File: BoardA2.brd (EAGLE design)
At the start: 44 x 93 mm, 18 parts, among them J1 FEMALE 2x3, T1 2N2222

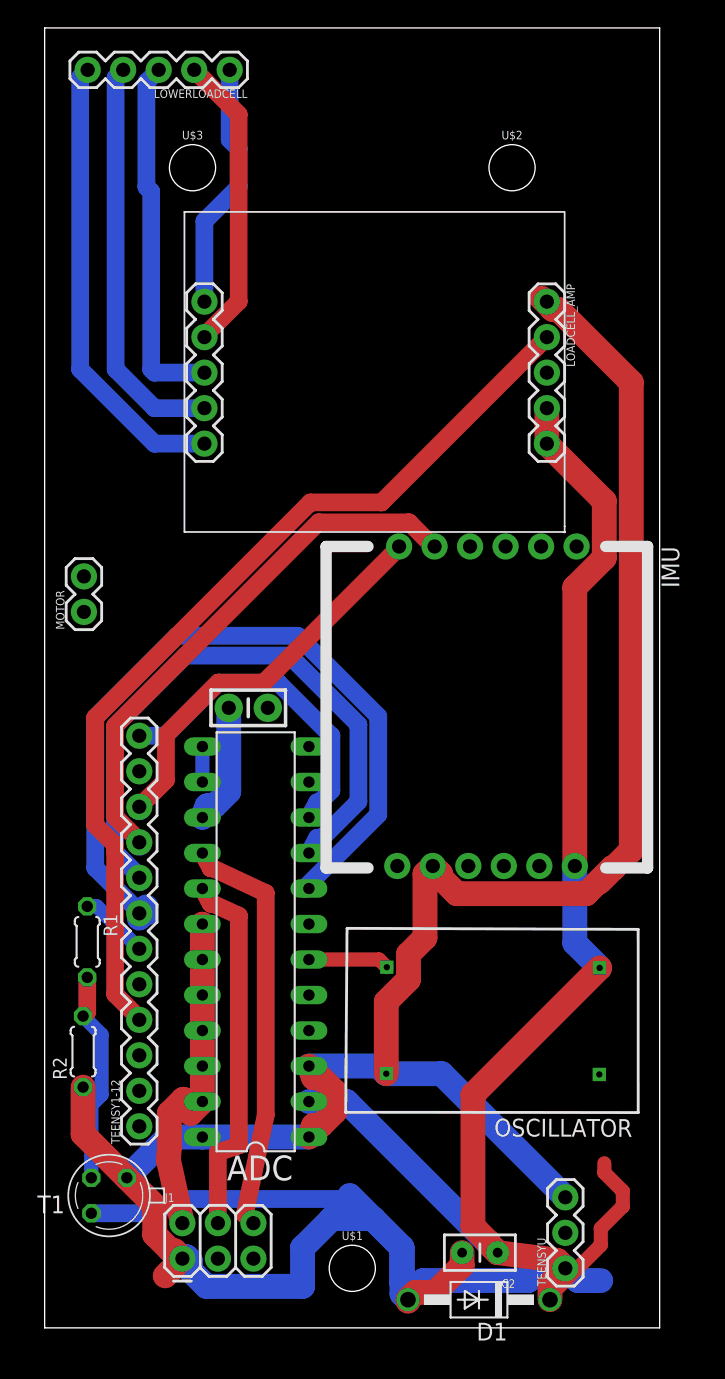
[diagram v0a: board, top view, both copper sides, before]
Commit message: moved connector board 1
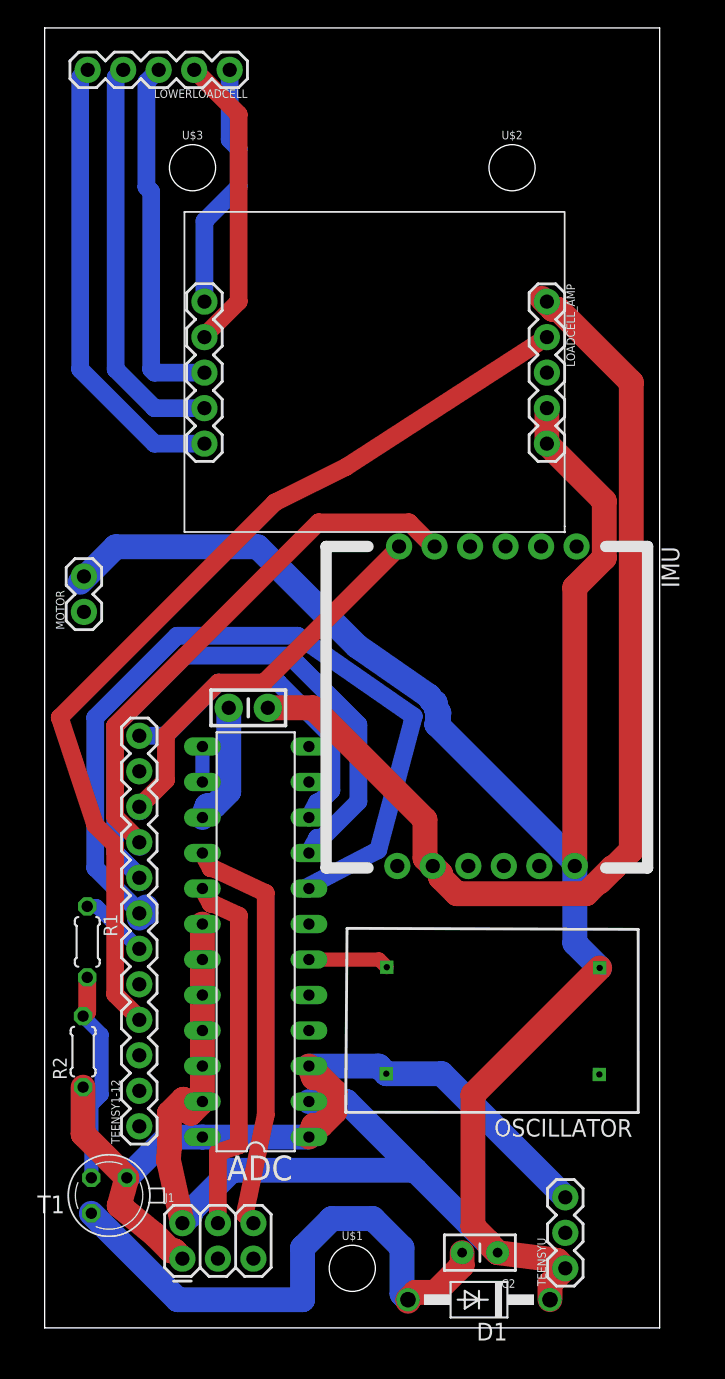
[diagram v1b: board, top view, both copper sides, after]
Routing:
- net 5V: track 158.2 -> 183.4 mm
- net N$6: track 46.0 -> 40.0 mm
- net ADC-TFS: track 56.7 -> 60.0 mm
- net AMP-CLK: track 66.5 -> 67.9 mm
- net GND: track 137.2 -> 137.8 mm

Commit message: Update 2
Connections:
- new net DC-CTRL: J1.2
- net 5V: now also J1.6; no longer J1.2
- net ADC-CH1: now also J1.5; no longer J1.6
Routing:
- net 5V: track 183.4 -> 173.6 mm
- net ADC-CH1: track 29.6 -> 28.7 mm
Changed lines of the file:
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@@
 <dimension x1="0" y1="0" x2="0" y2="93" x3="-13.335" y3="46.5" textsize="1.778" layer="1"/>
 <wire x1="0" y1="93" x2="0" y2="0" width="0" layer="20"/>
-<wire x1="1.5" y1="3.5" x2="42" y2="0.96" width="0.1524" layer="231"/>
+<wire x1="1.5" y1="0.96" x2="42" y2="0.96" width="0.1524" layer="231"/>
 <wire x1="42" y1="0.96" x2="42" y2="91.5" width="0.1524" layer="231"/>
 <wire x1="42" y1="91.5" x2="1.5" y2="91.5" width="0.1524" layer="231"/>
-<wire x1="1.5" y1="91.5" x2="1.5" y2="3.5" width="0.1524" layer="231"/>
+<wire x1="1.5" y1="91.5" x2="1.5" y2="0.96" width="0.1524" layer="231"/>
 </plain>
 <attributes>
@@
 <wire x1="11.287" y1="18.732" x2="11.287" y2="21.272" width="1.778" layer="1"/>
 <wire x1="35.932" y1="63.26" x2="35.932" y2="65.8" width="1.778" layer="1"/>
-<contactref element="J1" pad="2"/>
 <wire x1="11.287" y1="18.732" x2="11.287" y2="16.192" width="1.778" layer="1"/>
 <wire x1="37.93" y1="33.044" x2="37.93" y2="52.97515625" width="1.778" layer="1"/>
@@
 <wire x1="10.4488" y1="15.3538" x2="9.9216875" y2="16.3538" width="1.778" layer="1"/>
 <wire x1="8.9248" y1="12.9470875" x2="8.8552" y2="12.0166875" width="1.778" layer="1"/>
-<wire x1="8.8552" y1="12.0166875" x2="9.8552" y2="7.493" width="1.778" layer="1"/>
 <contactref element="MOTOR" pad="2"/>
-<wire x1="10.414" y1="8.31364375" x2="10.414" y2="8.0518" width="1.778" layer="16"/>
-<wire x1="10.414" y1="8.0518" x2="9.8552" y2="7.493" width="1.778" layer="16"/>
-<wire x1="26.515" y1="11.275" x2="13.37535625" y2="11.275" width="1.778" layer="16"/>
-<wire x1="13.37535625" y1="11.275" x2="10.414" y2="8.31364375" width="1.778" layer="16"/>
 <wire x1="28.1810875" y1="43.3644125" x2="28.12404375" y2="43.6804625" width="1.778" layer="16"/>
 <wire x1="28.12404375" y1="43.6804625" x2="28.20646875" y2="43.990853125" width="1.778" layer="16"/>
@@
 <wire x1="15.24" y1="55.88" x2="5.08" y2="55.88" width="1.778" layer="16"/>
 <wire x1="5.08" y1="55.88" x2="2.54" y2="53.34" width="1.778" layer="16"/>
+<contactref element="J1" pad="6"/>
+<wire x1="26.515" y1="11.275" x2="18.7172" y2="11.275" width="1.524" layer="16"/>
+<wire x1="18.7172" y1="11.275" x2="14.9352" y2="7.493" width="1.524" layer="16"/>
 <wire x1="22.337965625" y1="48.782034375" x2="18.907" y2="41.592" width="0" layer="19" extent="16-16"/>
 <wire x1="2.811" y1="53.763" x2="2.54" y2="53.34" width="0" layer="19" extent="16-16"/>
+<wire x1="8.8552" y1="12.0166875" x2="14.9352" y2="7.493" width="0" layer="19" extent="1-1"/>
 </signal>
 <signal name="N$1">
@@
 <signal name="ADC-CH1">
 <contactref element="ADC" pad="16"/>
-<contactref element="J1" pad="6"/>
 <wire x1="11.287" y1="33.972" x2="11.8792" y2="32.8798" width="1.27" layer="1"/>
 <wire x1="11.8792" y1="32.8798" x2="12.0471" y2="32.8798" width="1.27" layer="1"/>
-<wire x1="14.3176" y1="8.1106" x2="14.9352" y2="7.493" width="1.27" layer="1"/>
 <wire x1="12.0471" y1="32.8798" x2="15.8176" y2="31.1093" width="1.27" layer="1"/>
 <wire x1="15.8176" y1="31.1093" x2="15.8176" y2="15.24" width="1.27" layer="1"/>
 <wire x1="15.8176" y1="15.24" x2="14.3176" y2="8.1106" width="1.27" layer="1"/>
+<contactref element="J1" pad="5"/>
+<wire x1="14.9352" y1="4.953" x2="14.3176" y2="8.1106" width="0" layer="19" extent="1-1"/>
 </signal>
 <signal name="ADC-CH2">
@@
 <wire x1="13.239" y1="85.0107375" x2="13.239" y2="90.002" width="1.27" layer="16"/>
 </signal>
+<signal name="DC-CTRL">
+<contactref element="J1" pad="2"/>
+</signal>
 </signals>

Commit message: Mid board Rerouting 1
Work in progress. Please do not commit any changes to Board2
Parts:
- moved C2 84.2 mm to (40.0, 89.2)
- moved T1 82.7 mm to (30.0, 88.2)
- moved D1 81.4 mm to (36.2, 83.3)
- moved R2 69.9 mm to (25.6, 85.8)
- moved R1 61.1 mm to (20.8, 86.0)
- moved OSCILLATOR 58.8 mm to (23.0, 80.1), turned to 269.8 degrees
- moved MOTOR 43.5 mm to (22.2, 90.2), turned to 0 degrees
- moved LOADCELL_AMP 13.5 mm to (11.7, 64.0), turned to 90 degrees
- moved IMU 12.1 mm to (43.6, 43.8)
- moved TEENSYU 4.21 mm to (33.1, 3.88)
- moved TEENSY1-12 3.84 mm to (3.05, 13.5)
- moved C1 3.23 mm to (14.6, 47.6), turned to 90 degrees
- moved J1 2.54 mm to (7.82, 3.43)
- moved ADC 2.07 mm to (13.6, 29.0), turned to 270 degrees
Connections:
- removed net ADC-SLK: TEENSY1-12.5
- removed net N$11: ADC.4
- removed net TEENSY1: TEENSY1-12.1
- net ADC-SCLK: now also TEENSY1-12.5
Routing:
- net 5V: track 173.6 -> 0.00 mm
- net GND: track 137.8 -> 0.00 mm
- net AMP-CLK: track 67.9 -> 0.00 mm
- net ADC-TFS: track 60.0 -> 0.00 mm
- net ADC-RFS: track 44.0 -> 0.00 mm
- net N$6: track 40.0 -> 0.00 mm
- net IMU-TX: track 38.8 -> 0.00 mm
- net E+: track 32.7 -> 0.00 mm
- net N$5: track 29.1 -> 0.00 mm
- net ADC-CH1: track 28.7 -> 0.00 mm
- net IMU-RX: track 28.4 -> 0.00 mm
- net ADC-CH2: track 26.5 -> 0.00 mm
- net N$7: track 25.8 -> 0.00 mm
- net ADC-DOUT: track 23.4 -> 0.00 mm
- net N$9: track 21.5 -> 0.00 mm
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
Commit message: rerouting 2
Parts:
- moved OSCILLATOR 62.1 mm to (32.1, 18.6), turned to 179.8 degrees
- moved C1 37.4 mm to (19.6, 10.5)
- moved IMU 27.6 mm to (21.3, 27.6), turned to 90 degrees
- moved D1 8.27 mm to (34.6, 75.2)
- moved TEENSYU 4.21 mm to (37.2, 4.26)
- moved R2 4.10 mm to (23.6, 82.2)
- moved TEENSY1-12 3.84 mm to (6.77, 14.4)
- moved R1 3.21 mm to (19.8, 83.0)
- moved MOTOR 2.54 mm to (19.7, 90.2)
- moved ADC 1.83 mm to (15.1, 30.0)
- moved T1 1.14 mm to (29.0, 87.7)
- moved LOADCELL_AMP 1.02 mm to (12.7, 64.0)
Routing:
- net GND: track 0.00 -> 176.6 mm
- net 5V: track 0.00 -> 168.3 mm
- net MOTOR: track 0.00 -> 73.3 mm, vias 0 -> 2
- net IMU-RX: track 0.00 -> 59.1 mm
- net AMP-DAT: track 0.00 -> 50.7 mm, vias 0 -> 1
- net IMU-TX: track 0.00 -> 48.7 mm, vias 0 -> 1
- net ADC-DIN: track 0.00 -> 44.6 mm, vias 0 -> 1
- net AMP-CLK: track 0.00 -> 41.5 mm
- net N$4: track 0.00 -> 37.6 mm, vias 0 -> 1
- net ADC-RFS: track 0.00 -> 36.7 mm
- net N$6: track 0.00 -> 32.6 mm
- net ADC-CH1: track 0.00 -> 24.8 mm
- net N$3: track 0.00 -> 23.7 mm, vias 0 -> 1
- net ADC-CH2: track 0.00 -> 22.9 mm
- net N$7: track 0.00 -> 16.9 mm
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
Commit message: update 2
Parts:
- moved C1 2.74 mm to (17.1, 9.49), turned to 180 degrees
- moved J1 0.77 mm to (7.35, 2.83)
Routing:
- net 5V: track 168.3 -> 214.4 mm
- net ADC-DOUT: track 0.16 -> 32.3 mm, vias 0 -> 1
- net N$3: track 23.7 -> 14.9 mm, vias 1 -> 0
- net ADC-CH1: track 24.8 -> 31.2 mm
- net GND: track 176.6 -> 180.3 mm
- net N$4: track 37.6 -> 34.6 mm
- net AMP-DAT: track 50.7 -> 52.3 mm
- net ADC-CH2: track 22.9 -> 23.5 mm

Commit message: update3
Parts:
- moved MOTOR 2.25 mm to (20.2, 88.0)
- moved LOWERLOADCELL 2.00 mm to (13.2, 88.0)
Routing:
- net N$7: track 16.9 -> 14.1 mm
- net N$5: track 14.8 -> 12.8 mm
- net E+: track 14.8 -> 12.8 mm
- net N$9: track 14.8 -> 13.0 mm
- net N$10: track 14.8 -> 13.6 mm
- net N$6: track 32.6 -> 31.9 mm
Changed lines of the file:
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@@
 <element name="D1" library="diode" library_urn="urn:adsk.eagle:library:210" package="DO41-10" value="1N4004" x="34.63" y="75.168" rot="R180"/>
 <element name="C2" library="SparkFun-Passives" package="CAP-PTH-SMALL2" value="0.1uf" x="40.028" y="89.202" rot="R180"/>
-<element name="MOTOR" library="SparkFun-Connectors" package="1X02" value="" x="19.683" y="90.189"/>
-<element name="LOWERLOADCELL" library="SparkFun-Connectors" package="1X05" value="" x="13.239" y="90.002" rot="R180"/>
+<element name="MOTOR" library="SparkFun-Connectors" package="1X02" value="" x="20.191" y="88"/>
+<element name="LOWERLOADCELL" library="SparkFun-Connectors" package="1X05" value="" x="13.239" y="88" rot="R180"/>
 </elements>
 <signals>
@@
 <wire x1="39.3549" y1="89.9753" x2="39.3549" y2="89.6771" width="1.778" layer="1"/>
 <wire x1="39.3549" y1="89.6771" x2="40.132" y2="88.9" width="1.778" layer="1"/>
-<wire x1="22.223" y1="90.189" x2="26.5362875" y2="90.189" width="1.778" layer="1"/>
-<wire x1="26.5362875" y1="90.189" x2="27.4161875" y2="91.0689" width="1.778" layer="1"/>
 <wire x1="27.4161875" y1="91.0689" x2="38.2613" y2="91.0689" width="1.778" layer="1"/>
 <wire x1="40.132" y1="88.9" x2="40.132" y2="89.202" width="1.778" layer="1"/>
@@
 <wire x1="18.0242875" y1="28.765" x2="18.907" y2="28.765" width="1.778" layer="16"/>
 <wire x1="13.6492" y1="17.9000875" x2="13.6492" y2="24.3899125" width="1.778" layer="16"/>
+<wire x1="22.731" y1="88" x2="24.3472875" y2="88" width="1.778" layer="1"/>
+<wire x1="24.3472875" y1="88" x2="27.4161875" y2="91.0689" width="1.778" layer="1"/>
 </signal>
 <signal name="N$1">
@@
 <wire x1="33.02" y1="86.36" x2="35.862" y2="89.202" width="1.27" layer="1"/>
 <wire x1="35.862" y1="89.202" x2="37.488" y2="89.202" width="1.27" layer="1"/>
-<wire x1="27.724" y1="86.43" x2="26.778" y2="87.376" width="1.27" layer="1"/>
-<wire x1="26.778" y1="87.376" x2="22.352" y2="87.376" width="1.27" layer="1"/>
-<wire x1="22.352" y1="87.376" x2="22.223" y2="87.505" width="1.27" layer="1"/>
-<wire x1="22.223" y1="87.505" x2="19.683" y2="90.189" width="1.27" layer="1"/>
+<wire x1="27.724" y1="86.43" x2="23.424025" y2="86.43" width="1.016" layer="1"/>
+<wire x1="23.424025" y1="86.43" x2="23.393825" y2="86.3998" width="1.016" layer="1"/>
+<wire x1="23.393825" y1="86.3998" x2="22.3918" y2="86.3998" width="1.016" layer="1"/>
+<wire x1="22.3918" y1="86.3998" x2="21.844" y2="85.852" width="1.016" layer="1"/>
+<wire x1="21.844" y1="85.852" x2="21.844" y2="86.347" width="1.016" layer="1"/>
+<wire x1="21.844" y1="86.347" x2="20.191" y2="88" width="1.016" layer="1"/>
 </signal>
 <signal name="N$8">
@@
 <contactref element="LOWERLOADCELL" pad="5"/>
 <wire x1="7.634" y1="77.087" x2="3.079" y2="81.642" width="1.27" layer="1"/>
-<wire x1="3.079" y1="81.642" x2="3.079" y2="90.002" width="1.27" layer="1"/>
+<wire x1="3.079" y1="81.642" x2="3.079" y2="88" width="1.27" layer="1"/>
 </signal>
 <signal name="N$5">
 <contactref element="LOADCELL_AMP" pad="9"/>
 <contactref element="LOWERLOADCELL" pad="4"/>
-<wire x1="10.174" y1="77.087" x2="10.174" y2="77.71" width="1.27" layer="1"/>
-<wire x1="10.174" y1="77.71" x2="5.588" y2="82.296" width="1.27" layer="1"/>
-<wire x1="5.588" y1="82.296" x2="5.588" y2="89.971" width="1.27" layer="1"/>
-<wire x1="5.588" y1="89.971" x2="5.619" y2="90.002" width="1.27" layer="1"/>
+<wire x1="5.619" y1="88" x2="5.619" y2="81.642" width="1.27" layer="1"/>
+<wire x1="5.619" y1="81.642" x2="10.174" y2="77.087" width="1.27" layer="1"/>
 </signal>
 <signal name="N$7">
 <contactref element="LOADCELL_AMP" pad="8"/>
 <contactref element="LOWERLOADCELL" pad="3"/>
-<wire x1="12.714" y1="77.087" x2="12.714" y2="78.754" width="1.27" layer="16"/>
-<wire x1="12.714" y1="78.754" x2="15.24" y2="81.28" width="1.27" layer="16"/>
-<wire x1="11.9477375" y1="86.302" x2="11.859" y2="86.302" width="1.27" layer="16"/>
-<wire x1="11.859" y1="86.302" x2="8.159" y2="90.002" width="1.27" layer="16"/>
-<wire x1="15.24" y1="81.28" x2="15.24" y2="83.0097375" width="1.27" layer="16"/>
-<wire x1="15.24" y1="83.0097375" x2="11.9477375" y2="86.302" width="1.27" layer="16"/>
+<wire x1="8.159" y1="88" x2="8.159" y2="85.2487375" width="1.27" layer="16"/>
+<wire x1="8.159" y1="85.2487375" x2="7.278" y2="84.3677375" width="1.27" layer="16"/>
+<wire x1="7.278" y1="84.3677375" x2="7.278" y2="81.6322625" width="1.27" layer="16"/>
+<wire x1="7.278" y1="81.6322625" x2="9.2122625" y2="79.698" width="1.27" layer="16"/>
+<wire x1="9.2122625" y1="79.698" x2="10.103" y2="79.698" width="1.27" layer="16"/>
+<wire x1="10.103" y1="79.698" x2="12.714" y2="77.087" width="1.27" layer="16"/>
 </signal>
 <signal name="N$9">
 <contactref element="LOADCELL_AMP" pad="7"/>
 <contactref element="LOWERLOADCELL" pad="2"/>
-<wire x1="15.254" y1="77.087" x2="15.254" y2="85.33" width="1.27" layer="1"/>
-<wire x1="15.254" y1="85.33" x2="14.732" y2="85.852" width="1.27" layer="1"/>
-<wire x1="14.732" y1="85.852" x2="14.732" y2="85.969" width="1.27" layer="1"/>
-<wire x1="14.732" y1="85.969" x2="10.699" y2="90.002" width="1.27" layer="1"/>
+<wire x1="15.254" y1="77.087" x2="15.254" y2="83.806" width="1.27" layer="1"/>
+<wire x1="15.254" y1="83.806" x2="14.732" y2="84.328" width="1.27" layer="1"/>
+<wire x1="14.732" y1="84.328" x2="14.371" y2="84.328" width="1.27" layer="1"/>
+<wire x1="14.371" y1="84.328" x2="10.699" y2="88" width="1.27" layer="1"/>
 </signal>
 <signal name="N$10">
 <contactref element="LOADCELL_AMP" pad="6"/>
 <contactref element="LOWERLOADCELL" pad="1"/>
-<wire x1="17.794" y1="77.087" x2="17.794" y2="85.447" width="1.27" layer="1"/>
-<wire x1="17.794" y1="85.447" x2="13.239" y2="90.002" width="1.27" layer="1"/>
+<wire x1="17.794" y1="77.087" x2="17.794" y2="84.314" width="1.27" layer="1"/>
+<wire x1="17.794" y1="84.314" x2="13.716" y2="88.392" width="1.27" layer="1"/>
+<wire x1="13.716" y1="88.392" x2="13.631" y2="88.392" width="1.27" layer="1"/>
+<wire x1="13.631" y1="88.392" x2="13.239" y2="88" width="1.27" layer="1"/>
 </signal>
 <signal name="DC-CTRL">
